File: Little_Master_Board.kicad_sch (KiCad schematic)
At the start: 13 parts, among them J1 02x07 Header, J2 01x02 Header, J3 2.5mm Audio Jack, U1 SP3222EUEY-L_TR

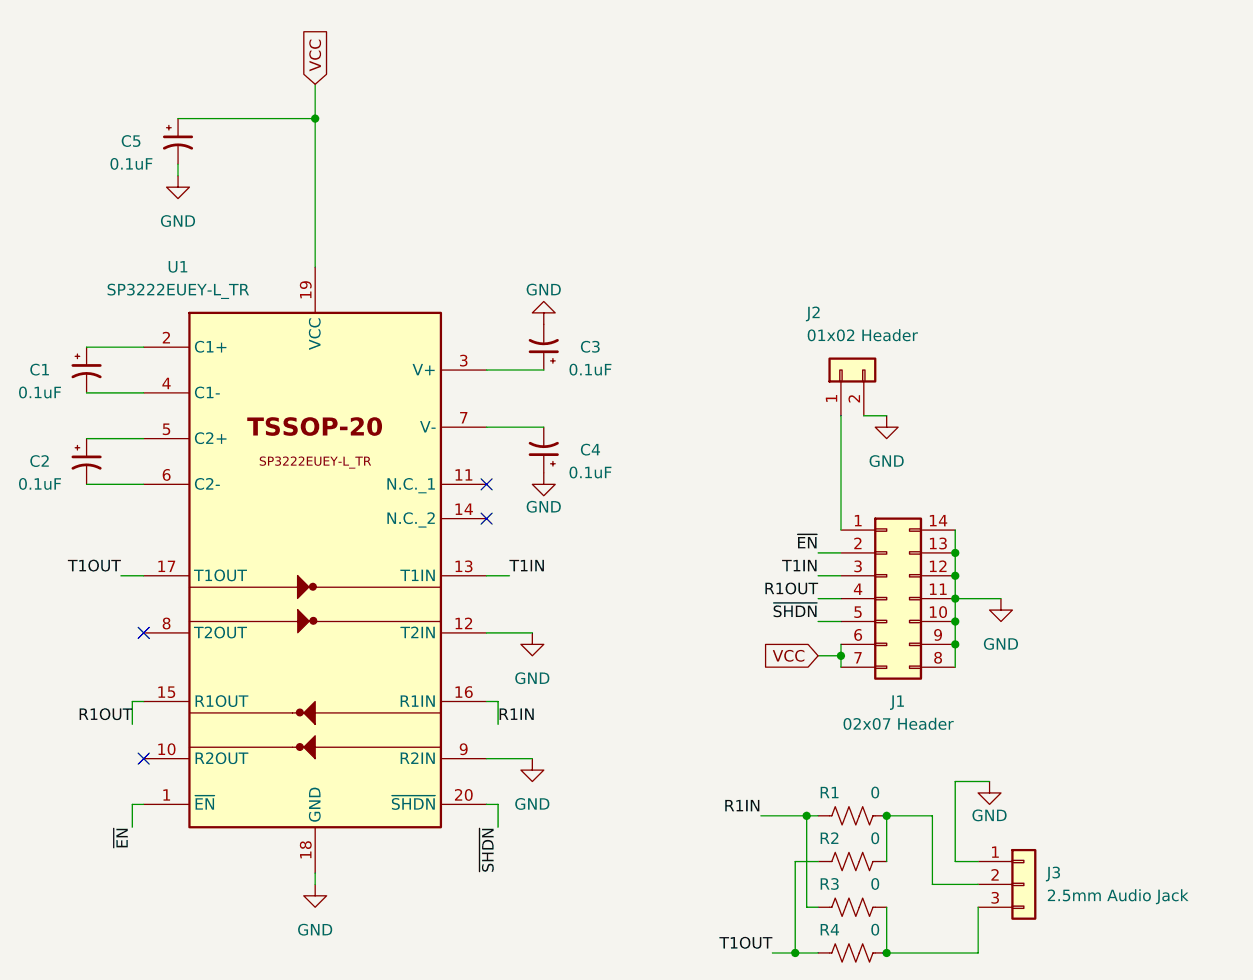
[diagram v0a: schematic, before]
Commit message: Fab files for Rev B updated. Removed SHDN on pin. Connected to VCC for HIGH. Added 2 pin header to pin 2 on 2x7 header. EN routed to pin 5 on 2x7 header.
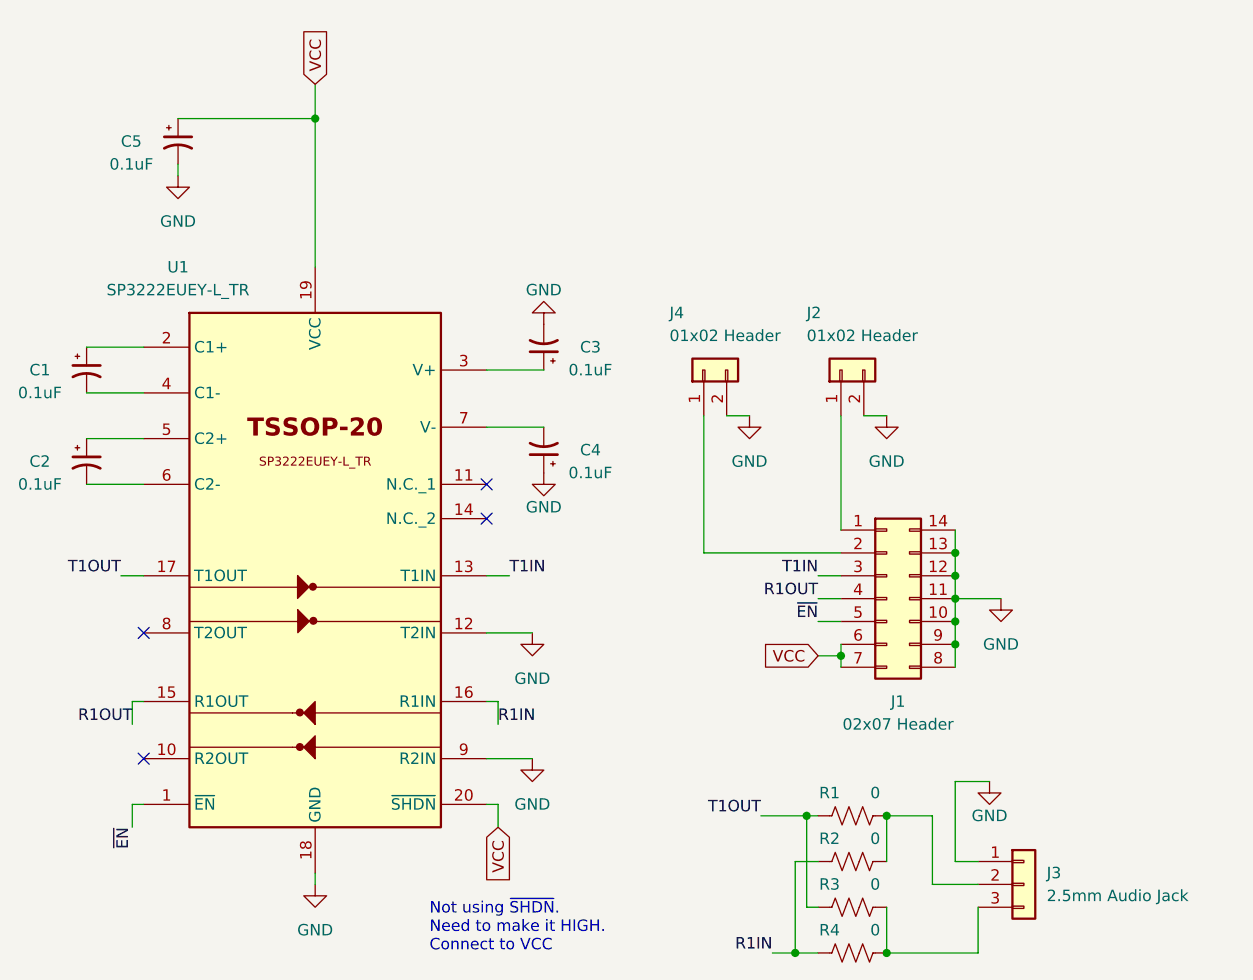
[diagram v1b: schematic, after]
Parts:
- added J4: 01x02 Header, Connector_PinHeader_2.54mm:PinHeader_1x02_P2.54mm_Vertical, symbol Connector_Generic:Conn_01x02
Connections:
- net GND: now also J4.2 (Pin_2)
- net R1IN: now also R2.1, R4.1; no longer R1.1, R3.1
- net T1OUT: now also R1.1, R3.1; no longer R2.1, R4.1
- net VCC: now also U1.20 (~{SHDN})
- net ~{EN}: now also J1.5 (Pin_5); no longer J1.2 (Pin_2)
- removed net ~{SHDN}: J1.5 (Pin_5), U1.20 (~{SHDN})
- new net: J1.2 (Pin_2), J4.1 (Pin_1)
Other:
- note added: "Not using ~{SHDN}. Need to make it HIGH. Connect to VCC"
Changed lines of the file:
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@@
+    (stroke (width 0) (type default))
+  )
+  (wire (pts (xy 161.29 67.31) (xy 161.29 82.55))
     (stroke (width 0) (type default))
   )
@@
     (stroke (width 0) (type default))
   )
-  (wire (pts (xy 173.99 82.55) (xy 176.53 82.55))
+  (wire (pts (xy 161.29 82.55) (xy 176.53 82.55))
     (stroke (width 0) (type default))
   )
@@
     (stroke (width 0) (type default))
   )
+  (wire (pts (xy 163.83 67.31) (xy 166.37 67.31))
+    (stroke (width 0) (type default))
+  )
   (wire (pts (xy 189.23 92.71) (xy 189.23 95.25))
     (stroke (width 0) (type default))
@@
     (stroke (width 0) (type default))
   )
+  (text "Not using ~{SHDN}.\nNeed to make it HIGH.\nConnect to VCC"
+    (at 130.81 127 0)
+    (effects (font (size 1.27 1.27)) (justify left bottom))
+  )
   (label "T1OUT" (at 96.52 85.09 180) (fields_autoplaced)
-    (effects (font (size 1.27 1.27)) (justify right bottom))
-  )
-  (label "~{EN}" (at 173.99 82.55 180) (fields_autoplaced)
-    (effects (font (size 1.27 1.27)) (justify right bottom))
-  )
-  (label "~{SHDN}" (at 173.99 90.17 180) (fields_autoplaced)
     (effects (font (size 1.27 1.27)) (justify right bottom))
   )
@@
     (effects (font (size 1.27 1.27)) (justify left bottom))
   )
-  (label "T1OUT" (at 168.91 127 180) (fields_autoplaced)
+  (label "T1OUT" (at 167.64 111.76 180) (fields_autoplaced)
     (effects (font (size 1.27 1.27)) (justify right bottom))
   )
@@
     (effects (font (size 1.27 1.27)) (justify right bottom))
   )
-  (label "R1IN" (at 167.64 111.76 180) (fields_autoplaced)
+  (label "~{EN}" (at 173.99 90.17 180) (fields_autoplaced)
+    (effects (font (size 1.27 1.27)) (justify right bottom))
+  )
+  (label "R1IN" (at 168.91 127 180) (fields_autoplaced)
     (effects (font (size 1.27 1.27)) (justify right bottom))
   )
@@
   )
   (label "R1OUT" (at 97.79 101.6 180) (fields_autoplaced)
-    (effects (font (size 1.27 1.27)) (justify right bottom))
-  )
-  (label "~{SHDN}" (at 138.43 113.03 270) (fields_autoplaced)
     (effects (font (size 1.27 1.27)) (justify right bottom))
   )
@@
     )
   )
+  (global_label "VCC" (shape input) (at 138.43 113.03 270) (fields_autoplaced)
+    (effects (font (size 1.27 1.27)) (justify right))
+    (property "Intersheetrefs" "${INTERSHEET_REFS}" (at 138.43 119.6438 90)
+      (effects (font (size 1.27 1.27)) (justify right) hide)
+    )
+  )
   (global_label "VCC" (shape input) (at 118.11 30.48 90) (fields_autoplaced)
     (effects (font (size 1.27 1.27)) (justify left))
     (property "Intersheetrefs" "${INTERSHEET_REFS}" (at 118.11 23.8662 90)
       (effects (font (size 1.27 1.27)) (justify left) hide)
+    )
+  )
+  (symbol (lib_id "power:GND") (at 166.37 67.31 0) (unit 1)
+    (in_bom yes) (on_board yes) (dnp no) (fields_autoplaced)
+    (property "Reference" "#PWR08" (at 166.37 73.66 0)
+      (effects (font (size 1.27 1.27)) hide)
+    )
+    (property "Value" "GND" (at 166.37 72.39 0)
+      (effects (font (size 1.27 1.27)))
+    )
+    (property "Footprint" "" (at 166.37 67.31 0)
+      (effects (font (size 1.27 1.27)) hide)
+    )
+    (property "Datasheet" "" (at 166.37 67.31 0)
+      (effects (font (size 1.27 1.27)) hide)
+    )
+    (pin "1")
+    (instances
+      (project "Little_Master_Board"
+        (path "/60da812d-4c66-4179-aeb1-84b5dae3f6cf"
+          (reference "#PWR08") (unit 1)
+        )
+      )
     )
   )
@@
         )
       )
+    )
+  )
+  (symbol (lib_id "Connector_Generic:Conn_01x02") (at 161.29 62.23 90) (unit 1)
+    (in_bom yes) (on_board yes) (dnp no)
+    (property "Reference" "J4" (at 157.48 55.88 90)
+      (effects (font (size 1.27 1.27)) (justify right))
+    )
+    (property "Value" "01x02 Header" (at 157.48 58.42 90)
+      (effects (font (size 1.27 1.27)) (justify right))
+    )
+    (property "Footprint" "Connector_PinHeader_2.54mm:PinHeader_1x02_P2.54mm_Vertical" (at 161.29 62.23 0)
+      (effects (font (size 1.27 1.27)) hide)
+    )
+    (property "Datasheet" "~" (at 161.29 62.23 0)
+      (effects (font (size 1.27 1.27)) hide)
+    )
+    (pin "1")
+    (pin "2")
+    (instances
+      (project "Little_Master_Board"
+        (path "/60da812d-4c66-4179-aeb1-84b5dae3f6cf"
+          (reference "J4") (unit 1)
+        )
+      )
